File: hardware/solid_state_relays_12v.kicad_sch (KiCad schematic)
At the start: 78 parts, among them J1 1190297, J2 1190297, J3 1190297, J4 1190297, J5 1190297, J6 1190297, J7 1190297, J8 1190297, Q1 IRF4905PBF, Q2 IRF4905PBF, Q3 IRF4905PBF, Q4 IRF4905PBF, Q5 IRF4905PBF, Q6 IRF4905PBF, Q7 IRF4905PBF, Q8 IRF4905PBF

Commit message: WIP control connector changes
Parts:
- removed JCNTL1: Conn_01x12, Connector_JST:JST_GH_SM12B-GHS-TB_1x12-1MP_P1.25mm_Horizontal, symbol dragon_mobile:Conn_01x12
- removed JP2: Conn_01x02, dragon_mobile:PinHeader_1x02_P1.00mm_Vertical, symbol Connector_Generic:Conn_01x02
- removed TVSP1, TVSP2: SM6T30AY, dragon_mobile:SMBJ36CATR, symbol dragon_mobile:SM6T30AY
- added FID1, FID2, FID3: Fiducial, Fiducial:Fiducial_0.5mm_Mask1mm, symbol Mechanical:Fiducial
- added JCNTL1, JCNTL2: Conn_02x05_Odd_Even, dragon_mobile:PinHeader_2x05_P1.27mm_Vertical, symbol Connector_Generic:Conn_02x05_Odd_Even
- added JP2: Conn_01x02, dragon_mobile:PinHeader_1x02_P1.00mm_Vertical, symbol dragon_mobile:Conn_01x02
- added JPWR2: XT60PW-M, dragon_mobile:XT60PWM, symbol dragon_mobile:XT60PW-M
- added TVSP1, TVSP2: SM6T16V5AY, dragon_mobile:SMBJ36CATR, symbol dragon_mobile:SM6T33AY
- HQ1, HQ2, HQ3, HQ4, HQ5, HQ6, HQ7, HQ8: value HeatsinkHole -> Access Hole; footprint MountingHole:MountingHole_3.2mm_M3_Pad_Via -> dragon_mobile:MountingHole_6.1mm_Pad_Via
- JL1, JL2, JL3, JL4, JL5, JL6, JL7, JL8: symbol Connector_Generic:Conn_01x02 -> dragon_mobile:Conn_01x02
- R1, RL1, RL2, RL3, RL4, RL5, RL6, RL7, RL8: value 1k5 -> 680; Characteristics Thick Film Resistor – 1.5KΩ 5% 500mW; Anti Surge AEC-Q200; 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 -> Thick Film Resistor – 680Ω 5% 500mW; Anti Surge AEC-Q200; 2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; Height (mm) 0.65 -> 0.55; MFP SDR10EZPJ152 -> SDR10EZPJ681; Mouser Part Number 755-SDR10EZPJ152 -> 755-SDR10EZPJ681; Mouser Price/Stock https://www.mouser.com/ProductDetail/ROHM-Semiconductor/SDR10EZPJ152?qs=MyNHzdoqoQKBvqImLWLCnQ%3D%3D -> https://www.mouser.com/ProductDetail/ROHM-Semiconductor/SDR10EZPJ681?qs=MyNHzdoqoQLanw95owtKRg%3D%3D
- TVS1, TVS2, TVS3, TVS4, TVS5, TVS6, TVS7, TVS8: value SM6T30AY -> SM6T16V5AY; Characteristics Uni-Directional TVS Diode, 30V 600W peak, 2-Pin DO-214AA SM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 -> Uni-Directional TVS Diode, 16V breakdown, 600W peak, 2-Pin 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; MFP SM6T30AY -> SM6T16V5AY; Mouser Part Number 511-SM6T30AY -> 511-SM6T16V5AY; Mouser Price/Stock https://www.mouser.com/ProductDetail/STMicroelectronics/SM6T30AY?qs=94V4QatVK%252BenipaHouN2sw%3D%3D -> https://www.mouser.com/ProductDetail/STMicroelectronics/SM6T16V5AY?qs=Ok1pvOkw6%2FqerKXvbVNOWA%3D%3D
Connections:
- net +BATT: now also JCNTL1.9 (Pin_9), JCNTL2.1 (Pin_1), JPWR2.P, TVSP1.1, TVSP2.1
- net GNDPWR: now also JCNTL1.10 (Pin_10), JCNTL1.2 (Pin_2), JCNTL1.4 (Pin_4), JCNTL1.6 (Pin_6), JCNTL1.8 (Pin_8), JCNTL2.2 (Pin_2), JCNTL2.4 (Pin_4), JCNTL2.6 (Pin_6), JCNTL2.7 (Pin_7), JCNTL2.9 (Pin_9), JP2.1 (Pin_1), JPWR2.N, TVSP1.2, TVSP2.2
- net a1: now also JCNTL1.1 (Pin_1)
- net a2: now also JCNTL1.3 (Pin_3)
- net a3: now also JCNTL1.7 (Pin_7)
- net a4: now also JCNTL1.5 (Pin_5)
- net a5: now also JCNTL2.5 (Pin_5)
- net a6: now also JCNTL2.3 (Pin_3)
- net a7: now also JCNTL2.8 (Pin_8)
- net a8: now also JCNTL2.10 (Pin_10)
- net at LEDP1.2, R1.1: now also JP2.2 (Pin_2)
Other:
- note added: "Control In / Power Out"
- note added: "Control inputs are active LOW / open collector"
- note added: "Fiducials"

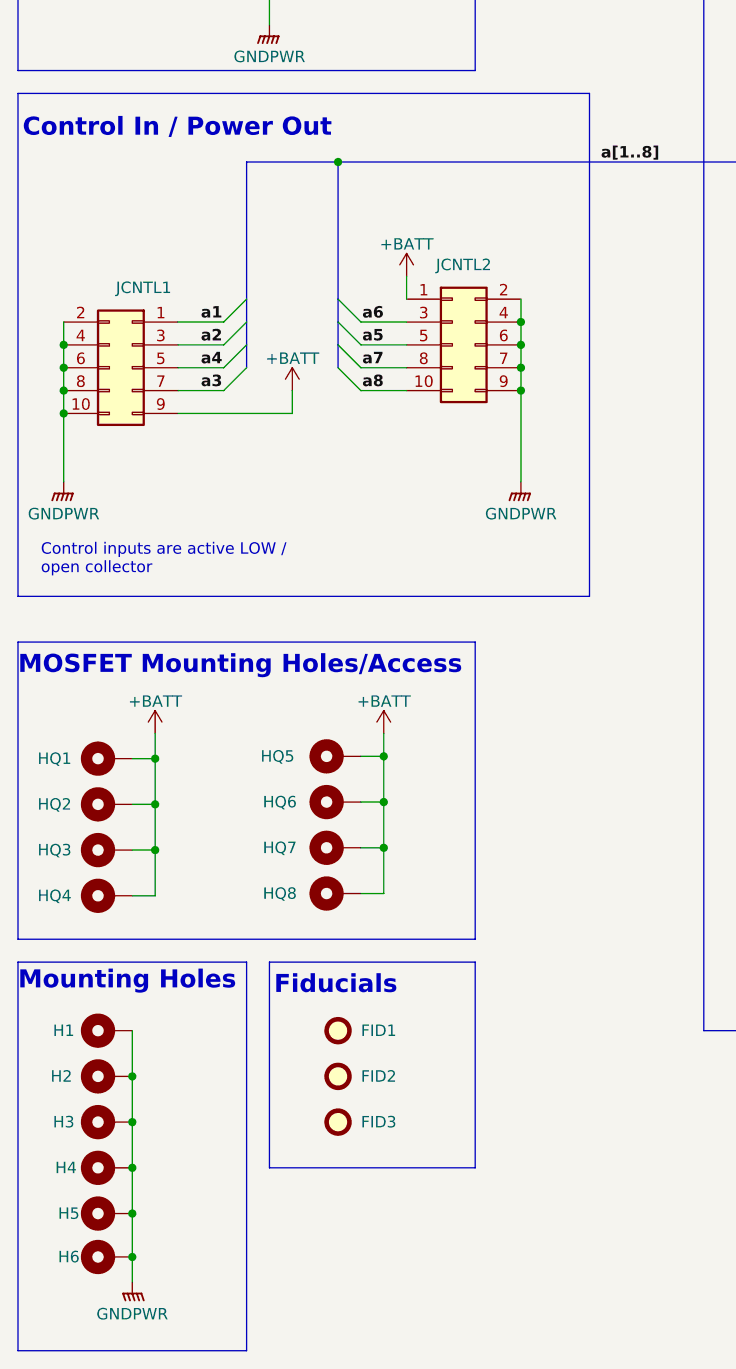
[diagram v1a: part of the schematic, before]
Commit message: Updated connectors and improved ground plane for control signals
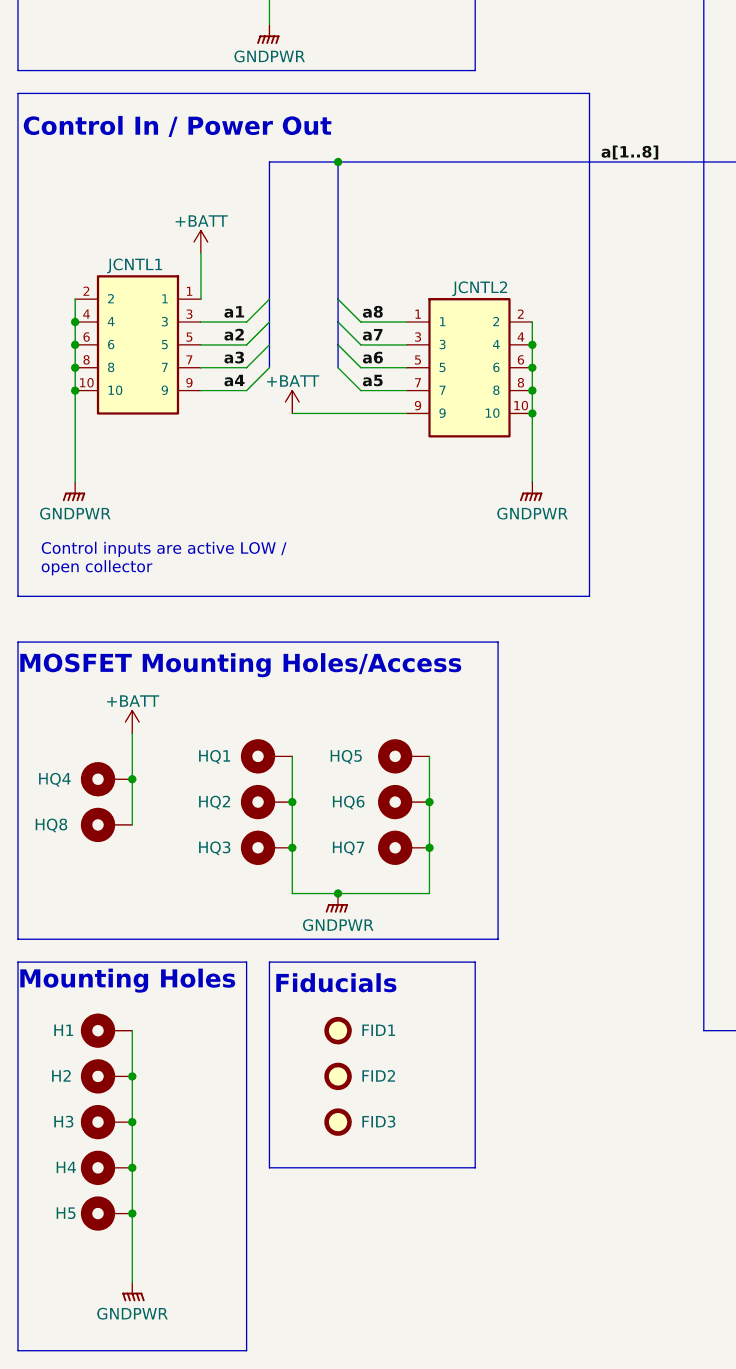
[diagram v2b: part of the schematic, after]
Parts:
- removed H6: MountingHole, MountingHole:MountingHole_3.2mm_M3_Pad_Via, symbol Mechanical:MountingHole_Pad
- JCNTL1, JCNTL2: value Conn_02x05_Odd_Even -> SHF-105-01-L-D-RA; footprint dragon_mobile:PinHeader_2x05_P1.27mm_Vertical -> dragon_mobile:SAMTEC_SHF-105-01-L-D-RA; symbol Connector_Generic:Conn_02x05_Odd_Even -> Connector_Samtec:SHF-105-01-L-D-RA; MANUFACTURER (none) -> Samtec; PARTREV (none) -> R; STANDARD (none) -> Manufacturer Recommendations
- TVSP2: Your Instructions/Notes (none) -> Reverse (Back) side mounted
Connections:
- net +BATT: now also JCNTL1.1, JCNTL2.9; no longer HQ1.1, HQ2.1, HQ3.1, HQ5.1, HQ6.1, HQ7.1, JCNTL1.9 (Pin_9), JCNTL2.1 (Pin_1)
- net GNDPWR: now also HQ1.1, HQ2.1, HQ3.1, HQ5.1, HQ6.1, HQ7.1, JCNTL2.10, JCNTL2.8; no longer JCNTL2.7 (Pin_7), JCNTL2.9 (Pin_9)
- net a1: now also JCNTL1.3; no longer JCNTL1.1 (Pin_1)
- net a2: now also JCNTL1.5; no longer JCNTL1.3 (Pin_3)
- net a4: now also JCNTL1.9; no longer JCNTL1.5 (Pin_5)
- net a5: now also JCNTL2.7; no longer JCNTL2.5 (Pin_5)
- net a6: now also JCNTL2.5; no longer JCNTL2.3 (Pin_3)
- net a7: now also JCNTL2.3; no longer JCNTL2.8 (Pin_8)
- net a8: now also JCNTL2.1; no longer JCNTL2.10 (Pin_10)
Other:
- moved on the sheet: HQ1, HQ2, HQ3, HQ4, HQ5, HQ6, HQ7, HQ8, JCNTL1, JCNTL2

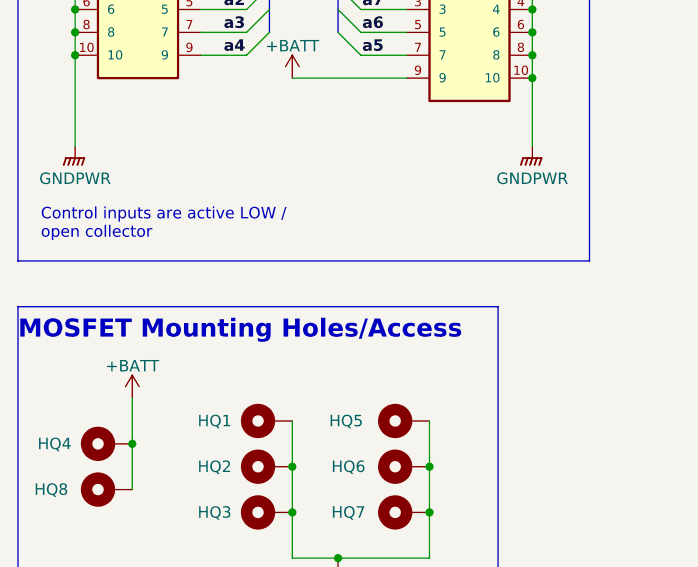
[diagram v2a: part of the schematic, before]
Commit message: Misc updates mostly related to Silkscreen and adding draft production output
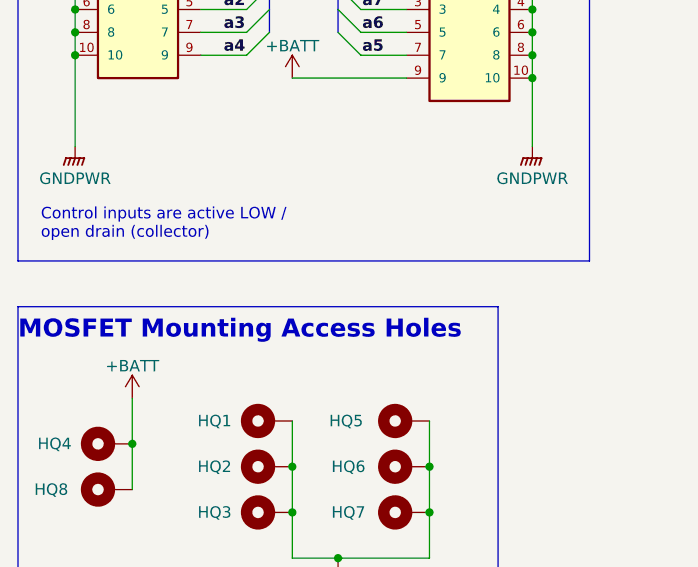
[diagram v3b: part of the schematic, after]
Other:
- note added: "Control inputs are active LOW / open drain (collector)"
- note added: "MOSFET Mounting Access Holes"
- note removed: "Control inputs are active LOW / open collector"
- note removed: "MOSFET Mounting Holes/Access"
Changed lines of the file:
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@@
   (title_block
     (title "Solid State Relays 12V")
-    (date "2022-12-22")
+    (date "2023-01-04")
     (rev "0.0.7")
     (comment 2 "creativecommons.org/licenses/by/4.0/")
@@
     )
   )
-  (text "MOSFET Mounting Holes/Access" (at 15.24 128.27 0)
+  (text "MOSFET Mounting Access Holes" (at 15.24 128.27 0)
     (effects (font (size 2 2) bold) (justify left bottom))
   )
-  (text "Control inputs are active LOW /\nopen collector" (at 17.78 117.094 0)
+  (text "Control inputs are active LOW /\nopen drain (collector)"
+    (at 17.78 117.094 0)
     (effects (font (size 1.27 1.27)) (justify left bottom))
   )

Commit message: Updated rev. to v0.0.8
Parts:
- JCNTL1, JCNTL2: Height (mm) (none) -> 5.33
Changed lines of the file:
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@@
   (title_block
     (title "Solid State Relays 12V")
-    (date "2023-01-04")
-    (rev "0.0.7")
+    (date "2023-01-10")
+    (rev "0.0.8")
     (comment 2 "creativecommons.org/licenses/by/4.0/")
     (comment 3 "License: CC By 4.0")
@@
     )
   )
-  (symbol (lib_name "SHF-105-01-L-D-RA_1") (lib_id "Connector_Samtec:SHF-105-01-L-D-RA") (at 28.575 91.44 0) (mirror y) (unit 1)
+  (symbol (lib_id "Connector_Samtec:SHF-105-01-L-D-RA") (at 28.575 91.44 0) (mirror y) (unit 1)
     (in_bom yes) (on_board yes)
     (property "Reference" "JCNTL1" (id 0) (at 28.321 82.55 0))
@@
       (effects (font (size 1.27 1.27)) (justify bottom) hide)
     )
-    (property "Datasheet" "~" (id 3) (at 28.575 91.44 0)
+    (property "Datasheet" "https://www.mouser.com/datasheet/2/527/shf-2854584.pdf" (id 3) (at 28.575 91.44 0)
       (effects (font (size 1.27 1.27)) hide)
     )
@@
       (effects (font (size 1.27 1.27)) (justify bottom) hide)
     )
+    (property "Description" "Headers & Wire Housings Shrouded Terminal Strip, 0.050\"(1.27mm) pitch, Pin(Male), Right Angle, IDC; 10 Pos. 2 Rows;" (id 7) (at -19.05 121.92 0)
+      (effects (font (size 1.27 1.27)) hide)
+    )
+    (property "Height (mm)" "5.33" (id 8) (at 37.465 119.38 0))
     (pin "1")
     (pin "10")
@@
       (effects (font (size 1.27 1.27)) (justify bottom) hide)
     )
-    (property "Datasheet" "~" (id 3) (at 65.405 93.98 0)
+    (property "Datasheet" "https://www.mouser.com/datasheet/2/527/shf-2854584.pdf" (id 3) (at 65.405 93.98 0)
       (effects (font (size 1.27 1.27)) hide)
     )
@@
       (effects (font (size 1.27 1.27)) (justify bottom) hide)
     )
+    (property "Description" "Headers & Wire Housings Shrouded Terminal Strip, 0.050\"(1.27mm) pitch, Pin(Male), Right Angle, IDC; 10 Pos. 2 Rows;" (id 7) (at 113.03 124.46 0)
+      (effects (font (size 1.27 1.27)) hide)
+    )
+    (property "Height (mm)" "5.33" (id 8) (at 56.515 121.92 0))
     (pin "1")
     (pin "10")

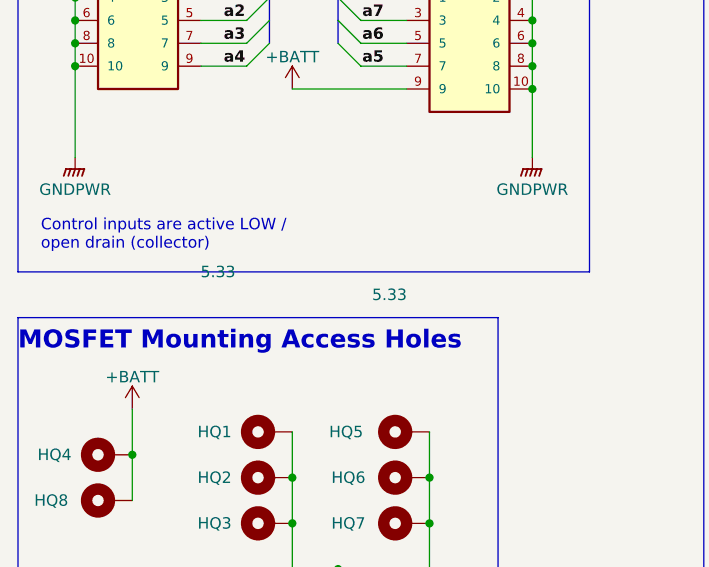
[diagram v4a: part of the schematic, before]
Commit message: Updated production files for v0.0.9
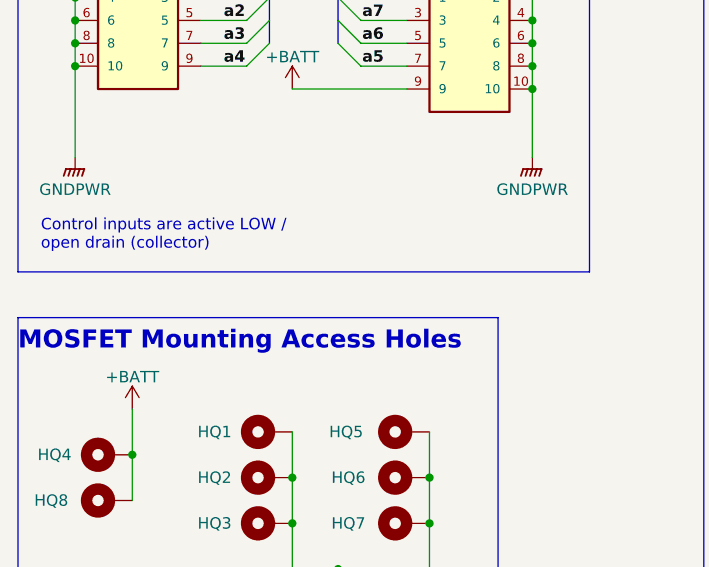
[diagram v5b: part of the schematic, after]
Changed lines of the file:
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@@
     (title "Solid State Relays 12V")
     (date "2023-01-10")
-    (rev "0.0.8")
+    (rev "0.0.9")
     (comment 2 "creativecommons.org/licenses/by/4.0/")
     (comment 3 "License: CC By 4.0")
@@
       (effects (font (size 1.27 1.27)) hide)
     )
-    (property "Height (mm)" "5.33" (id 8) (at 37.465 119.38 0))
+    (property "Height (mm)" "5.33" (id 8) (at 37.465 119.38 0)
+      (effects (font (size 1.27 1.27)) hide)
+    )
     (pin "1")
     (pin "10")
@@
       (effects (font (size 1.27 1.27)) hide)
     )
-    (property "Height (mm)" "5.33" (id 8) (at 56.515 121.92 0))
+    (property "Height (mm)" "5.33" (id 8) (at 56.515 121.92 0)
+      (effects (font (size 1.27 1.27)) hide)
+    )
     (pin "1")
     (pin "10")
